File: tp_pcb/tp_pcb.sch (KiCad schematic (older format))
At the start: 23 parts, among them K0 KEYSW, K1 KEYSW, K2 KEYSW, K3 KEYSW, K4 KEYSW, K5 KEYSW, K6 KEYSW, P0 CONN_01X08, P1 CONN_01X08, P2 CONN_01X06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

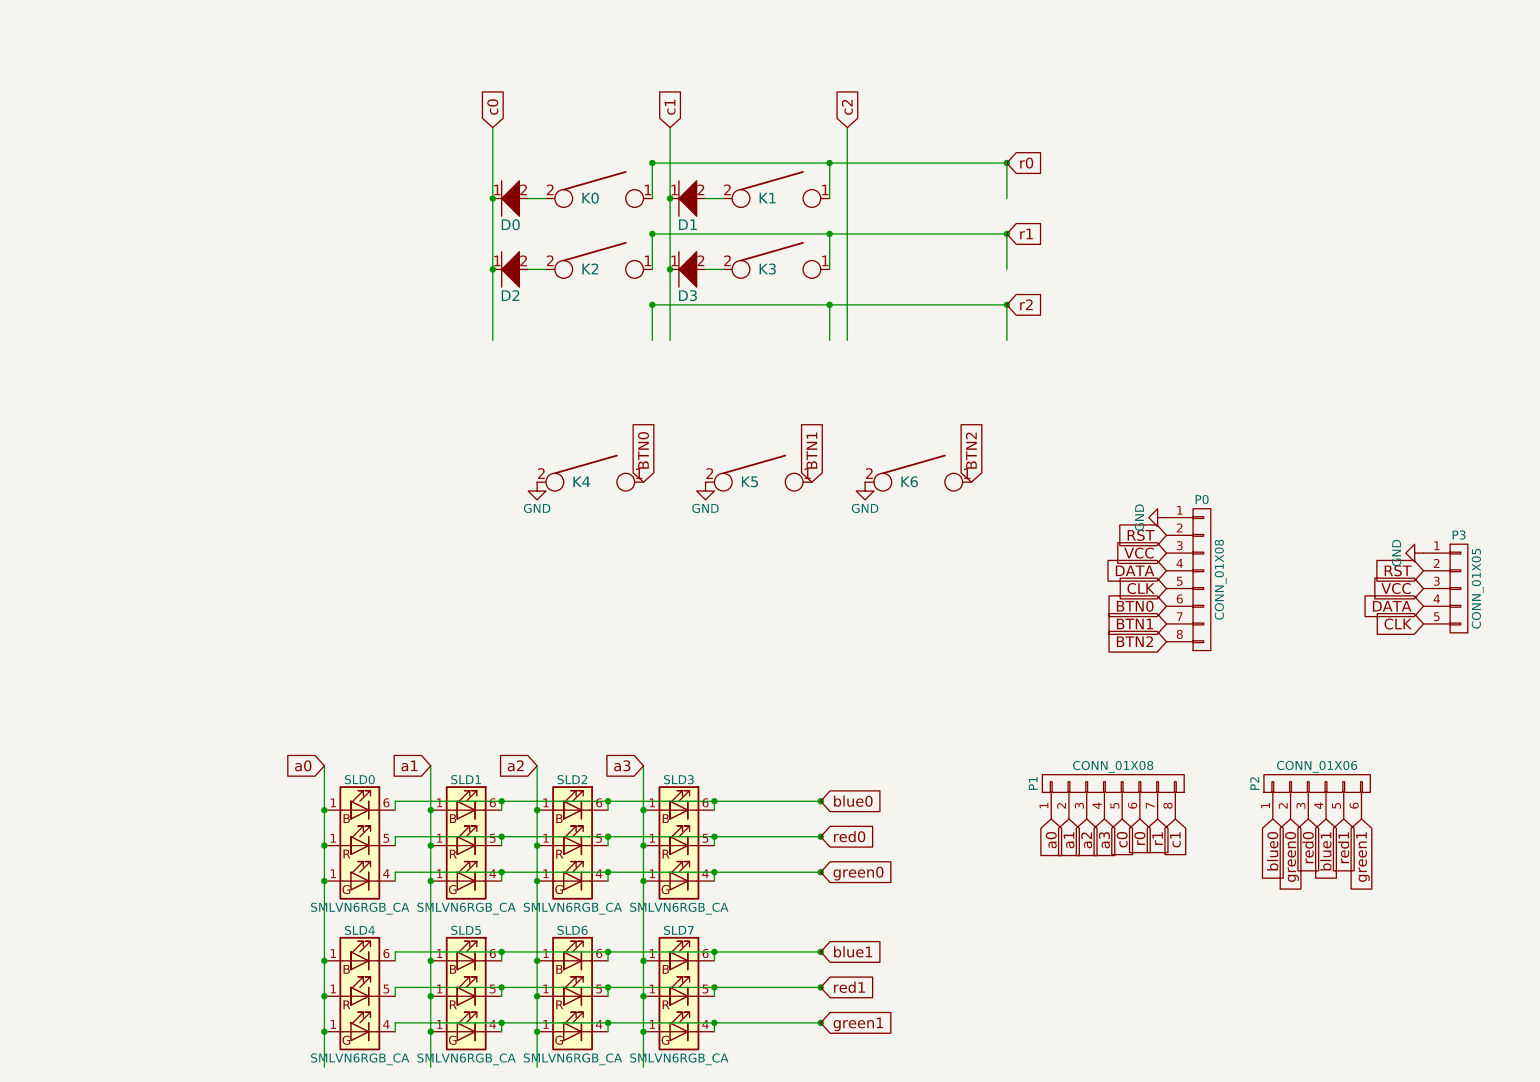
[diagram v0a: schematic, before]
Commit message: working on mounting holes
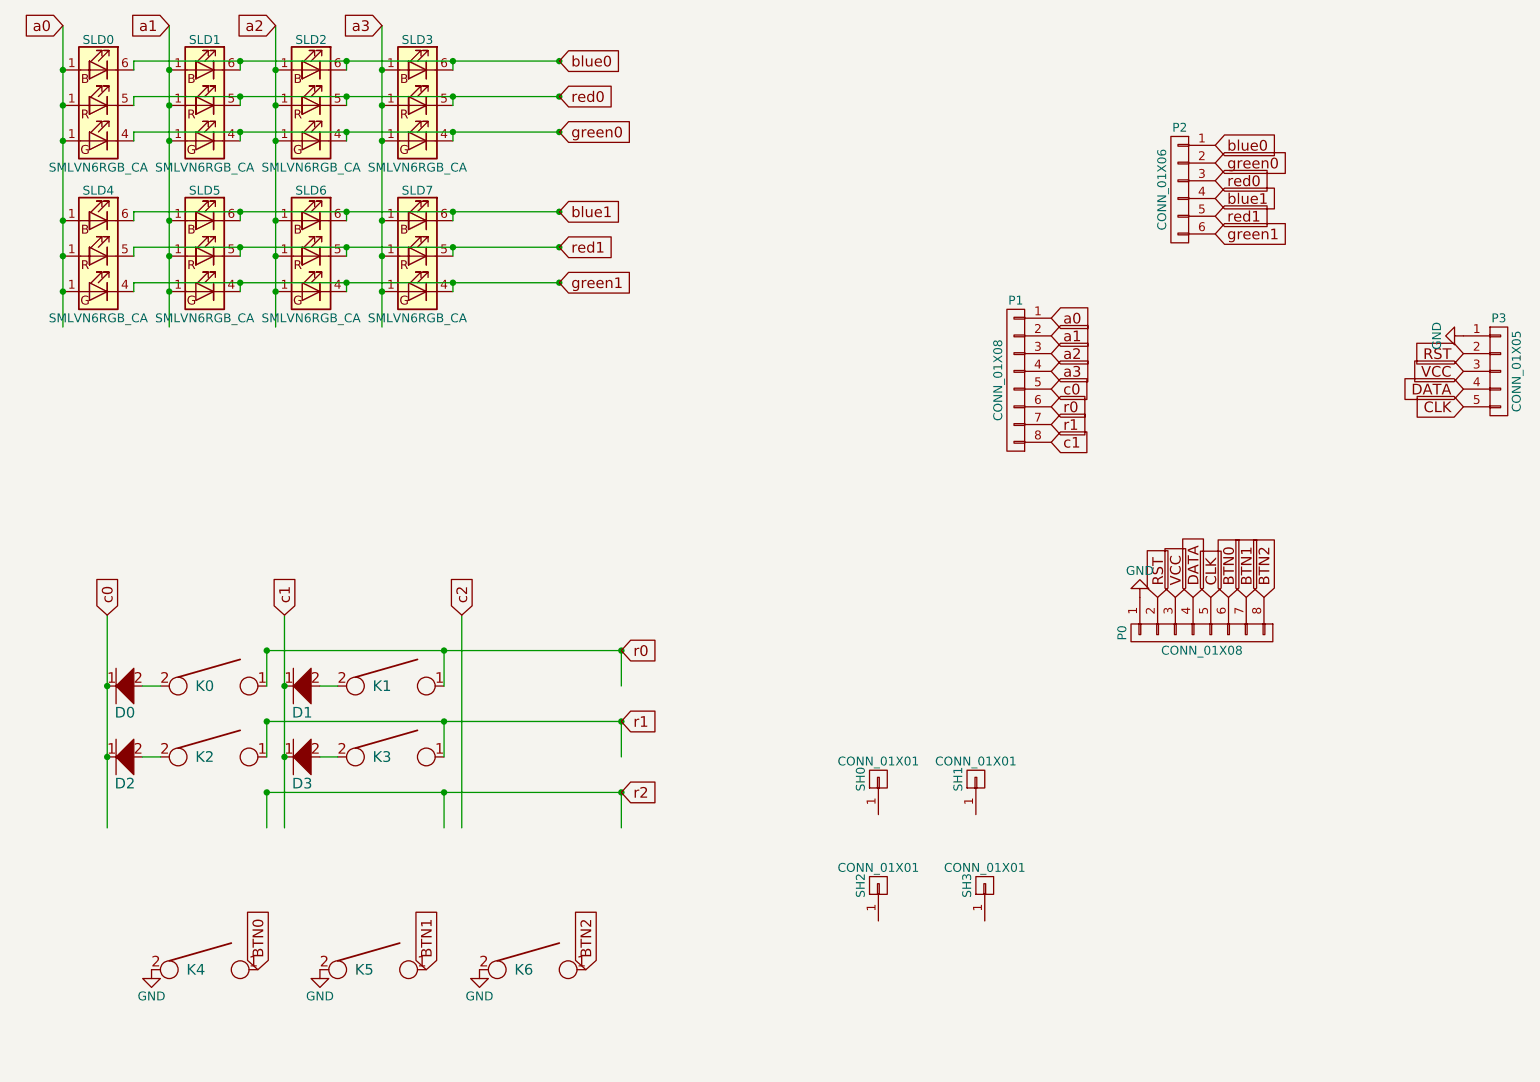
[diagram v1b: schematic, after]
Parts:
- added SH0, SH1, SH2, SH3: CONN_01X01, Mounting_Holes:MountingHole_2.5mm, symbol CONN_01X01
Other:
- moved on the sheet: D0, D1, D2, D3, K0, K1, K2, K3, K4, K5, K6, P0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

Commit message: tp adjusted mounting hole text
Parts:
- SH0, SH1, SH2, SH3: footprint Mounting_Holes:MountingHole_2.5mm -> cherry_rgb:MOUNTING_HOLE
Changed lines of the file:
@@
 F 0 "SH0" H 5875 5575 50  0000 C CNN
 F 1 "CONN_01X01" V 5975 5475 50  0000 C CNN
-F 2 "Mounting_Holes:MountingHole_2.5mm" H 5875 5475 50  0001 C CNN
+F 2 "cherry_rgb:MOUNTING_HOLE" H 5875 5475 50  0001 C CNN
 F 3 "" H 5875 5475 50  0000 C CNN
 	1    5875 5475
@@
 F 0 "SH1" H 6425 5575 50  0000 C CNN
 F 1 "CONN_01X01" V 6525 5475 50  0000 C CNN
-F 2 "Mounting_Holes:MountingHole_2.5mm" H 6425 5475 50  0001 C CNN
+F 2 "cherry_rgb:MOUNTING_HOLE" H 6425 5475 50  0001 C CNN
 F 3 "" H 6425 5475 50  0000 C CNN
 	1    6425 5475
@@
 F 0 "SH2" H 5875 6175 50  0000 C CNN
 F 1 "CONN_01X01" V 5975 6075 50  0000 C CNN
-F 2 "Mounting_Holes:MountingHole_2.5mm" H 5875 6075 50  0001 C CNN
+F 2 "cherry_rgb:MOUNTING_HOLE" H 5875 6075 50  0001 C CNN
 F 3 "" H 5875 6075 50  0000 C CNN
 	1    5875 6075
@@
 F 0 "SH3" H 6475 6175 50  0000 C CNN
 F 1 "CONN_01X01" V 6575 6075 50  0000 C CNN
-F 2 "Mounting_Holes:MountingHole_2.5mm" H 6475 6075 50  0001 C CNN
+F 2 "cherry_rgb:MOUNTING_HOLE" H 6475 6075 50  0001 C CNN
 F 3 "" H 6475 6075 50  0000 C CNN
 	1    6475 6075

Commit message: tp groundplanes seem done
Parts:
- added V0, V1, V2, V3: CONN_01X01, cherry_rgb:VIA127, symbol CONN_01X01
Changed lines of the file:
@@
 	0    -1   -1   0
 $EndComp
+$Comp
+L CONN_01X01 V0
+U 1 1 58B33B38
+P 7625 5425
+F 0 "V0" H 7625 5525 50  0000 C CNN
+F 1 "CONN_01X01" V 7725 5425 50  0000 C CNN
+F 2 "cherry_rgb:VIA127" H 7625 5425 50  0001 C CNN
+F 3 "" H 7625 5425 50  0000 C CNN
+	1    7625 5425
+	0    -1   -1   0
+$EndComp
+$Comp
+L CONN_01X01 V1
+U 1 1 58B33B3E
+P 8175 5425
+F 0 "V1" H 8175 5525 50  0000 C CNN
+F 1 "CONN_01X01" V 8275 5425 50  0000 C CNN
+F 2 "cherry_rgb:VIA127" H 8175 5425 50  0001 C CNN
+F 3 "" H 8175 5425 50  0000 C CNN
+	1    8175 5425
+	0    -1   -1   0
+$EndComp
+$Comp
+L CONN_01X01 V2
+U 1 1 58B33B44
+P 7625 6025
+F 0 "V2" H 7625 6125 50  0000 C CNN
+F 1 "CONN_01X01" V 7725 6025 50  0000 C CNN
+F 2 "cherry_rgb:VIA127" H 7625 6025 50  0001 C CNN
+F 3 "" H 7625 6025 50  0000 C CNN
+	1    7625 6025
+	0    -1   -1   0
+$EndComp
+$Comp
+L CONN_01X01 V3
+U 1 1 58B33B4A
+P 8175 6025
+F 0 "V3" H 8175 6125 50  0000 C CNN
+F 1 "CONN_01X01" V 8275 6025 50  0000 C CNN
+F 2 "cherry_rgb:VIA127" H 8175 6025 50  0001 C CNN
+F 3 "" H 8175 6025 50  0000 C CNN
+	1    8175 6025
+	0    -1   -1   0
+$EndComp
+$Comp
+L GND #PWR06
+U 1 1 58B33D7A
+P 7625 5625
+F 0 "#PWR06" H 7625 5375 50  0001 C CNN
+F 1 "GND" H 7625 5475 50  0000 C CNN
+F 2 "" H 7625 5625 50  0000 C CNN
+F 3 "" H 7625 5625 50  0000 C CNN
+	1    7625 5625
+	-1   0    0    -1
+$EndComp
+$Comp
+L GND #PWR07
+U 1 1 58B33DE2
+P 8175 5625
+F 0 "#PWR07" H 8175 5375 50  0001 C CNN
+F 1 "GND" H 8175 5475 50  0000 C CNN
+F 2 "" H 8175 5625 50  0000 C CNN
+F 3 "" H 8175 5625 50  0000 C CNN
+	1    8175 5625
+	-1   0    0    -1
+$EndComp
+$Comp
+L GND #PWR08
+U 1 1 58B343A1
+P 7625 6225
+F 0 "#PWR08" H 7625 5975 50  0001 C CNN
+F 1 "GND" H 7625 6075 50  0000 C CNN
+F 2 "" H 7625 6225 50  0000 C CNN
+F 3 "" H 7625 6225 50  0000 C CNN
+	1    7625 6225
+	-1   0    0    -1
+$EndComp
+$Comp
+L GND #PWR09
+U 1 1 58B34409
+P 8175 6225
+F 0 "#PWR09" H 8175 5975 50  0001 C CNN
+F 1 "GND" H 8175 6075 50  0000 C CNN
+F 2 "" H 8175 6225 50  0000 C CNN
+F 3 "" H 8175 6225 50  0000 C CNN
+	1    8175 6225
+	-1   0    0    -1
+$EndComp
 $EndSCHEMATC

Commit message: tp silkscreen touchup and a few final tweaks
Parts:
- removed SH0, SH1, SH2, SH3: CONN_01X01, cherry_rgb:MOUNTING_HOLE, symbol CONN_01X01
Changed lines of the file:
@@
-$EndComp
-$Comp
-L CONN_01X01 SH0
-U 1 1 58B3144D
-P 5875 5475
-F 0 "SH0" H 5875 5575 50  0000 C CNN
-F 1 "CONN_01X01" V 5975 5475 50  0000 C CNN
-F 2 "cherry_rgb:MOUNTING_HOLE" H 5875 5475 50  0001 C CNN
-F 3 "" H 5875 5475 50  0000 C CNN
-	1    5875 5475
-	0    -1   -1   0
-$EndComp
-$Comp
-L CONN_01X01 SH1
-U 1 1 58B3164A
-P 6425 5475
-F 0 "SH1" H 6425 5575 50  0000 C CNN
-F 1 "CONN_01X01" V 6525 5475 50  0000 C CNN
-F 2 "cherry_rgb:MOUNTING_HOLE" H 6425 5475 50  0001 C CNN
-F 3 "" H 6425 5475 50  0000 C CNN
-	1    6425 5475
-	0    -1   -1   0
-$EndComp
-$Comp
-L CONN_01X01 SH2
-U 1 1 58B316D9
-P 5875 6075
-F 0 "SH2" H 5875 6175 50  0000 C CNN
-F 1 "CONN_01X01" V 5975 6075 50  0000 C CNN
-F 2 "cherry_rgb:MOUNTING_HOLE" H 5875 6075 50  0001 C CNN
-F 3 "" H 5875 6075 50  0000 C CNN
-	1    5875 6075
-	0    -1   -1   0
-$EndComp
-$Comp
-L CONN_01X01 SH3
-U 1 1 58B317E5
-P 6475 6075
-F 0 "SH3" H 6475 6175 50  0000 C CNN
-F 1 "CONN_01X01" V 6575 6075 50  0000 C CNN
-F 2 "cherry_rgb:MOUNTING_HOLE" H 6475 6075 50  0001 C CNN
-F 3 "" H 6475 6075 50  0000 C CNN
-	1    6475 6075
-	0    -1   -1   0
 $EndComp
 $Comp
